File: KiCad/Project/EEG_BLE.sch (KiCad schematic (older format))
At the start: 5 parts

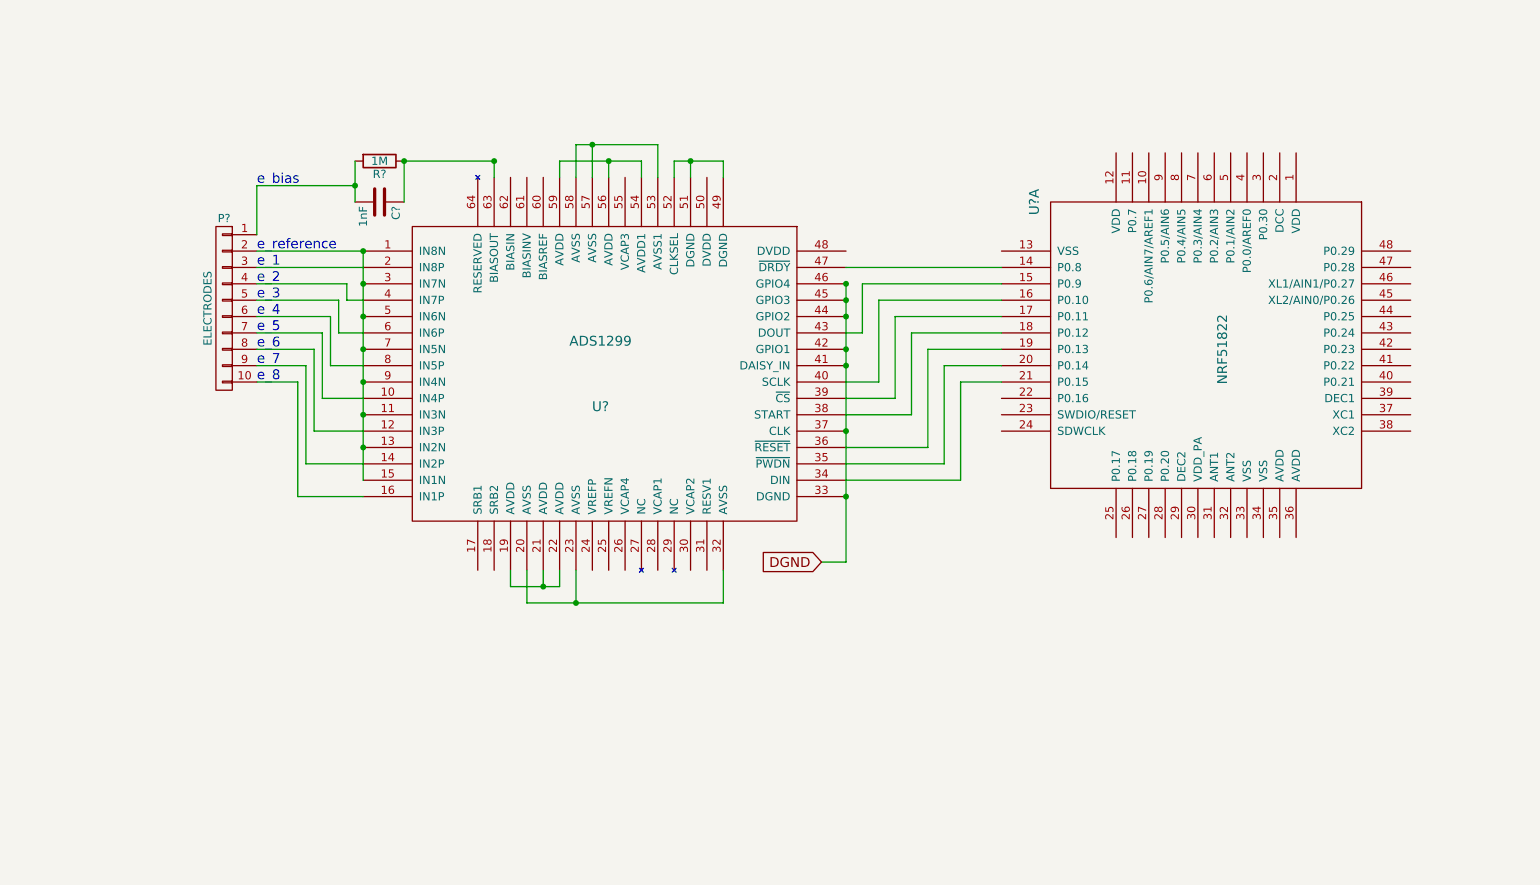
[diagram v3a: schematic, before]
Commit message: Adds decoupling capacitors to the schematics
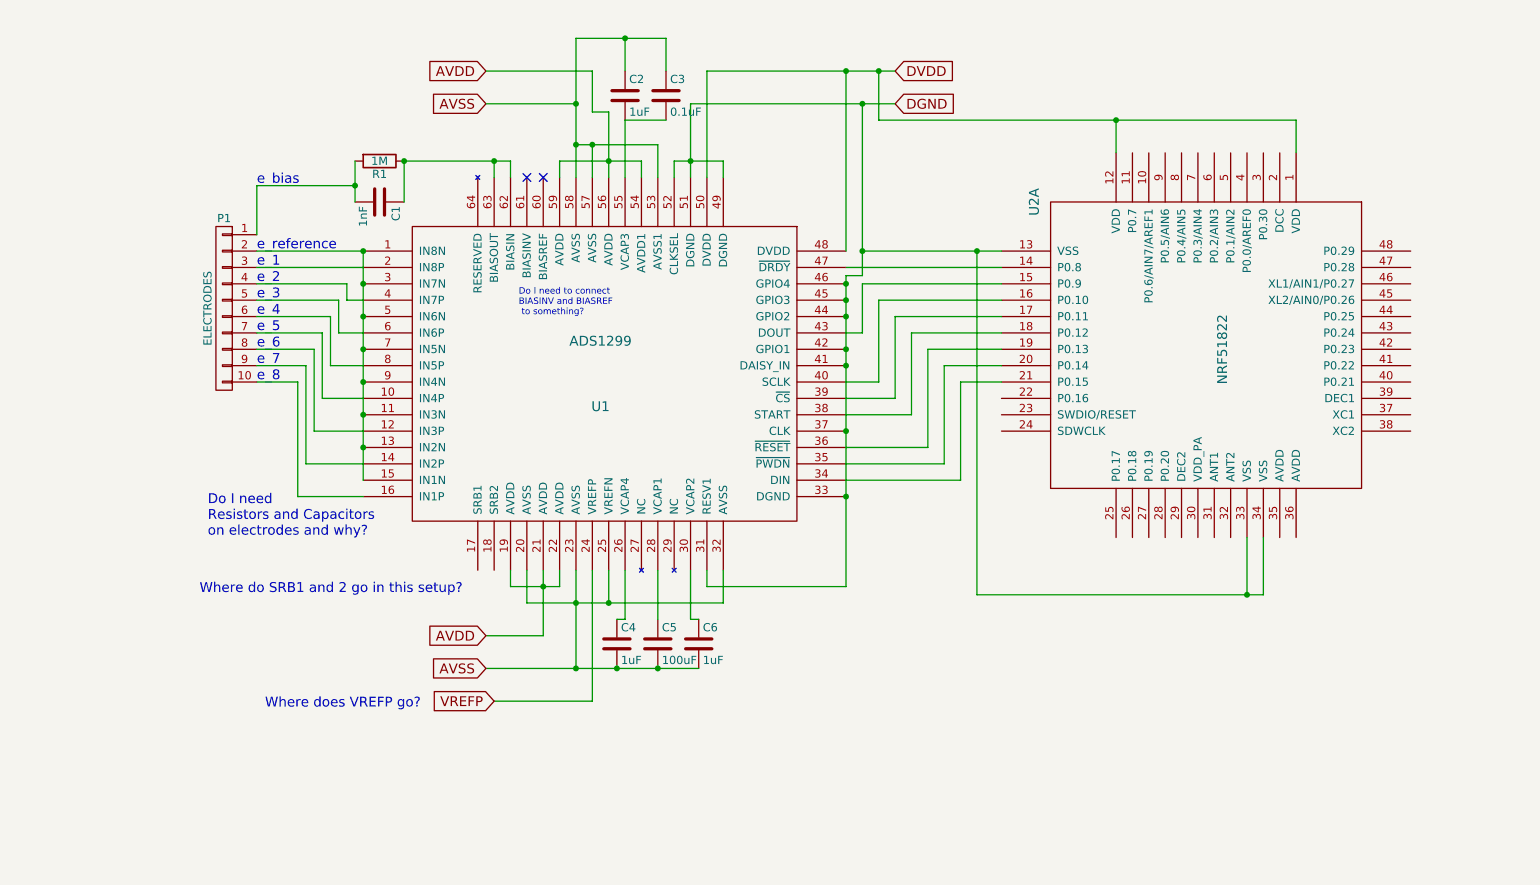
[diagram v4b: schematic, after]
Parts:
- added C2, C4, C6: 1uF, symbol C
- added C3: 0.1uF, symbol C
- added C5: 100uF, symbol C
- gave numbers to parts that had none: 5
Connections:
- net DGND: now also U1.31 (RESV1), U1.49 (DGND), U1.51 (DGND), U1.52 (CLKSEL), U2.13 (VSS), U2.33 (VSS), U2.34 (VSS)
- net AVDD: now reaches U1.19 (AVDD), U1.21 (AVDD), U1.22 (AVDD)
- net AVDD: now also U1.54 (AVDD1), U1.56 (AVDD), U1.59 (AVDD)
- net AVSS: now reaches U1.20 (AVSS), U1.23 (AVSS), U1.32 (AVSS)
- net AVSS: now also U1.25 (VREFN), U1.53 (AVSS1), U1.57 (AVSS), U1.58 (AVSS), C2.1, C3.1, C4.2, C5.2, C6.2
- net VREFP: now reaches U1.24 (VREFP)
- net at U1.26 (VCAP4): now also C4.1
- net at U1.28 (VCAP1): now also C5.1
- net at U1.30 (VCAP2): now also C6.1
- net DVDD: now reaches U1.48 (DVDD)
- net DVDD: now also U1.50 (DVDD), U2.1 (VDD), U2.12 (VDD)
- net at U1.55 (VCAP3): now also C2.2, C3.2
- net at U1.62 (BIASIN): now also C1.1, R1.1, U1.63 (BIASOUT)
- no-connect marks 0 -> 2
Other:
- note added: "Do I need \nResistors and Capacitors \non electrodes and why?"
- note added: "Do I need to connect \nBIASINV and BIASREF\n to something?"
- note added: "Where do SRB1 and 2 go in this setup?"
- note added: "Where does VREFP go?"
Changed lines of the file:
@@
 $EndDescr
 $Comp
-L NRF51822 U?
+L NRF51822 U2
 U 1 1 57D46615
 P 7950 3500
-F 0 "U?" H 6350 2000 60  0000 C CNN
+F 0 "U2" H 6350 2000 60  0000 C CNN
 F 1 "NRF51822" H 7250 3150 60  0000 C CNN
 F 2 "" H 7250 3150 60  0000 C CNN
@@
 $EndComp
 $Comp
-L R R?
+L R R1
 U 1 1 57D49926
 P 2450 1650
-F 0 "R?" V 2530 1650 50  0000 C CNN
+F 0 "R1" V 2530 1650 50  0000 C CNN
 F 1 "1M" V 2450 1650 50  0000 C CNN
 F 2 "" V 2380 1650 50  0000 C CNN
@@
 $EndComp
 $Comp
-L C C?
+L C C1
 U 1 1 57D5BB9F
 P 2450 1900
-F 0 "C?" H 2475 2000 50  0000 L CNN
+F 0 "C1" H 2475 2000 50  0000 L CNN
 F 1 "1nF" H 2475 1800 50  0000 L CNN
 F 2 "" H 2488 1750 50  0000 C CNN
@@
 $EndComp
 $Comp
-L ADS1299 U?
+L ADS1299 U1
 U 1 1 57D3263D
 P 3800 2950
-F 0 "U?" H 3800 2750 60  0000 C CNN
+F 0 "U1" H 3800 2750 60  0000 C CNN
 F 1 "ADS1299" H 3800 3150 60  0000 C CNN
 F 2 "" H 3800 2950 60  0001 C CNN
@@
 $EndComp
 $Comp
-L CONN_01X10 P?
+L CONN_01X10 P1
 U 1 1 57D5C6C1
 P 1500 2550
-F 0 "P?" H 1500 3100 50  0000 C CNN
+F 0 "P1" H 1500 3100 50  0000 C CNN
 F 1 "ELECTRODES" V 1600 2550 50  0000 C CNN
 F 2 "" H 1500 2550 50  0000 C CNN
@@
 Text Notes 1700 1800 0    60   ~ 0
 e_bias
+NoConn ~ 3350 1750
+$Comp
+L C C2
+U 1 1 57DCFDDF
+P 3950 1250
+F 0 "C2" H 3975 1350 50  0000 L CNN
+F 1 "1uF" H 3975 1150 50  0000 L CNN
+F 2 "" H 3988 1100 50  0000 C CNN
+F 3 "" H 3950 1250 50  0000 C CNN
+	1    3950 1250
+	1    0    0    -1
+$EndComp
+$Comp
+L C C4
+U 1 1 57DCFEE7
+P 3900 4600
+F 0 "C4" H 3925 4700 50  0000 L CNN
+F 1 "1uF" H 3925 4500 50  0000 L CNN
+F 2 "" H 3938 4450 50  0000 C CNN
+F 3 "" H 3900 4600 50  0000 C CNN
+	1    3900 4600
+	1    0    0    -1
+$EndComp
+$Comp
+L C C5
+U 1 1 57DCFF14
+P 4150 4600
+F 0 "C5" H 4175 4700 50  0000 L CNN
+F 1 "100uF" H 4175 4500 50  0000 L CNN
+F 2 "" H 4188 4450 50  0000 C CNN
+F 3 "" H 4150 4600 50  0000 C CNN
+	1    4150 4600
+	1    0    0    -1
+$EndComp
+$Comp
+L C C6
+U 1 1 57DCFF41
+P 4400 4600
+F 0 "C6" H 4425 4700 50  0000 L CNN
+F 1 "1uF" H 4425 4500 50  0000 L CNN
+F 2 "" H 4438 4450 50  0000 C CNN
+F 3 "" H 4400 4600 50  0000 C CNN
+	1    4400 4600
+	1    0    0    -1
+$EndComp
+Text GLabel 3100 4550 0    60   Input ~ 0
+AVDD
+Text GLabel 3100 4750 0    60   Input ~ 0
+AVSS
+Text GLabel 5600 1100 2    60   Input ~ 0
+DVDD
+Text GLabel 5600 1300 2    60   Input ~ 0
+DGND
+Text GLabel 3100 1100 0    60   Input ~ 0
+AVDD
+Text GLabel 3100 1300 0    60   Input ~ 0
+AVSS
+NoConn ~ 3450 1750
+$Comp
+L C C3
+U 1 1 57DDBFB3
+P 4200 1250
+F 0 "C3" H 4225 1350 50  0000 L CNN
+F 1 "0.1uF" H 4225 1150 50  0000 L CNN
+F 2 "" H 4238 1100 50  0000 C CNN
+F 3 "" H 4200 1250 50  0000 C CNN
+	1    4200 1250
+	1    0    0    -1
+$EndComp
+Text GLabel 3150 4950 0    60   Input ~ 0
+VREFP
+Connection ~ 7750 4300
+Wire Wire Line
+	7750 3950 7750 4300
+Connection ~ 6100 2200
+Wire Wire Line
+	6100 4300 6100 2200
+Wire Wire Line
+	7850 4300 6100 4300
+Wire Wire Line
+	7850 3950 7850 4300
+Connection ~ 5400 2200
+Wire Wire Line
+	5500 1400 5500 1100
+Connection ~ 6950 1400
+Wire Wire Line
+	6950 1600 6950 1400
+Wire Wire Line
+	8050 1400 5500 1400
+Wire Wire Line
+	8050 1600 8050 1400
+Connection ~ 5500 1100
+Wire Wire Line
+	5400 2200 6250 2200
+Wire Wire Line
+	3750 4950 3150 4950
+Wire Wire Line
+	3750 4150 3750 4950
+Connection ~ 3850 4350
+Wire Wire Line
+	3850 4150 3850 4350
+Wire Wire Line
+	3950 1400 4200 1400
+Connection ~ 3950 900
+Wire Wire Line
+	4200 900  4200 1100
+Wire Wire Line
+	3950 900  3950 1100
+Wire Wire Line
+	3650 900  4200 900
+Connection ~ 3650 1300
+Connection ~ 3900 4750
+Connection ~ 4150 4750
+Connection ~ 3650 4750
+Wire Wire Line
+	3750 1100 3100 1100
+Wire Wire Line
+	3750 1350 3750 1100
+Wire Wire Line
+	3750 1350 3850 1350
+Wire Wire Line
+	3650 1300 3100 1300
+Connection ~ 5400 1300
+Wire Wire Line
+	5400 2350 5400 1300
+Wire Wire Line
+	5300 2350 5400 2350
+Connection ~ 5300 1100
+Wire Wire Line
+	5300 2200 5300 1100
+Wire Wire Line
+	4450 1100 5600 1100
+Wire Wire Line
+	4450 1750 4450 1100
+Wire Wire Line
+	4350 1300 5600 1300
+Wire Wire Line
+	3100 4750 4400 4750
+Wire Wire Line
+	3450 4550 3100 4550
+Wire Wire Line
+	4450 4250 5300 4250
+Wire Wire Line
+	4450 4150 4450 4250
+Wire Wire Line
+	4350 4450 4350 4150
+Wire Wire Line
+	4400 4450 4350 4450
 Connection ~ 2600 1650
 Wire Wire Line
-	3150 1650 2600 1650
+	2600 1650 3250 1650
 Connection ~ 2350 2200
 Connection ~ 2350 2400
@@
 	3250 4250 3550 4250
 Wire Wire Line
-	3450 4250 3450 4150
+	3450 4150 3450 4550
 Wire Wire Line
 	3550 4250 3550 4150
@@
 	3350 4350 4550 4350
 Wire Wire Line
-	3650 4350 3650 4150
+	3650 4150 3650 4750
 Wire Wire Line
 	4550 4350 4550 4150
@@
 	3550 1650 4050 1650
 Wire Wire Line
-	3850 1650 3850 1750
+	3850 1350 3850 1750
 Wire Wire Line
 	4050 1650 4050 1750
 Connection ~ 3850 1650
 Wire Wire Line
-	3650 1750 3650 1550
+	3650 900  3650 1750
 Wire Wire Line
 	3650 1550 4150 1550
@@
 	4550 1650 4550 1750
 Wire Wire Line
-	4350 1750 4350 1650
+	4350 1300 4350 1750
 Connection ~ 4350 1650
 Wire Wire Line
-	5300 2400 5300 4100
-Text GLabel 5150 4100 0    60   Input ~ 0
-DGND
-Wire Wire Line
-	5300 4100 5150 4100
+	5300 2350 5300 4250
+Wire Wire Line
+	3250 1650 3250 1750
+Connection ~ 3650 1550
+Wire Wire Line
+	3950 1750 3950 1400
+Wire Wire Line
+	3900 4450 3950 4450
+Wire Wire Line
+	3950 4450 3950 4150
+Wire Wire Line
+	4150 4450 4150 4150
+Text Notes 1750 5000 0    60   ~ 0
+Where does VREFP go?
+Text Notes 1350 4300 0    60   ~ 0
+Where do SRB1 and 2 go in this setup?
+Text Notes 1400 3950 0    60   ~ 0
+Do I need \nResistors and Capacitors \non electrodes and why?
+Text Notes 3300 2600 0    39   ~ 0
+Do I need to connect \nBIASINV and BIASREF\n to something?
 $EndSCHEMATC

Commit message: Adds questions and power supplies draft
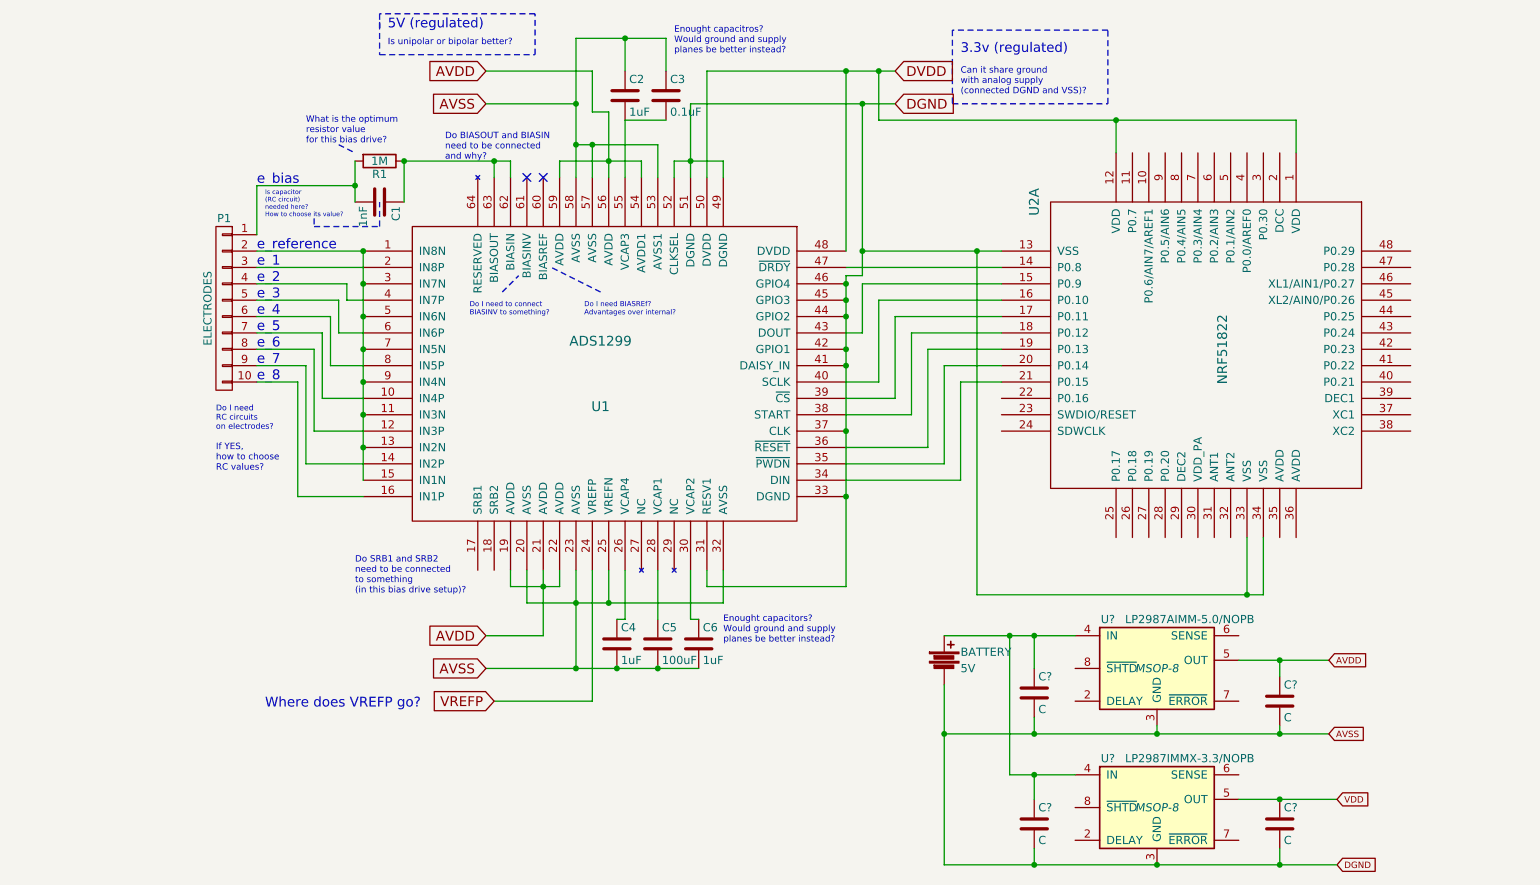
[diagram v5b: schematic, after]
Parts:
- added BATTERY: 5V, symbol Battery
- added C? (x4): C, symbol C
- added U?: LP2987AIMM-5.0/NOPB, MSOP-8, symbol LP2987AIMM-5.0/NOPB
- added U?: LP2987IMMX-3.3/NOPB, MSOP-8, symbol LP2987IMMX-3.3/NOPB
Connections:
- net DGND is gone; now on net AVSS: U1.31 (RESV1), U1.33 (DGND), U1.37 (CLK), U1.41 (DAISY_IN), U1.42 (GPIO1), U1.44 (GPIO2), U1.45 (GPIO3), U1.46 (GPIO4), U1.49 (DGND), U1.51 (DGND), U1.52 (CLKSEL), U2.13 (VSS), U2.33 (VSS), U2.34 (VSS)
- net AVDD: now also C?.1, U?.5 (OUT)
- net AVSS: now also BATTERY.2, C?.2, C?.2, C?.2, C?.2, U?.3 (GND), U?.3 (GND)
- new net: BATTERY.1, C?.1, C?.1, U?.4 (IN), U?.4 (IN)
- new net VDD: C?.1, U?.5 (OUT)
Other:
- note added: "3.3v (regulated)"
- note added: "5V (regulated)"
- note added: "Can it share ground \nwith analog supply \n(connected DGND and VSS)?"
- note added: "Do BIASOUT and BIASIN \nneed to be connected \nand why?"
- note added: "Do I need BIASREf?\nAdvantages over internal?"
- note added: "Do I need \nRC circuits\non electrodes?"
- note added: "Do I need to connect \nBIASINV to something?"
- note added: "Do SRB1 and SRB2 \nneed to be connected \nto something \n(in this bias drive setup)?"
- note added: "Enought capacitors?\nWould ground and supply \nplanes be better instead?"
- note added: "Enought capacitros?\nWould ground and supply \nplanes be better instead?"
- note added: "If YES, \nhow to choose \nRC values?"
- note added: "Is capacitor \n(RC circuit)\nneeded here? \nHow to choose its value?"
- note added: "Is unipolar or bipolar better?"
- note added: "What is the optimum \nresistor value \nfor this bias drive?"
- note removed: "Do I need \nResistors and Capacitors \non electrodes and why?"
- note removed: "Do I need to connect \nBIASINV and BIASREF\n to something?"
- note removed: "Where do SRB1 and 2 go in this setup?"
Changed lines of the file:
@@
-$EndComp
-$Comp
-L ADS1299 U1
-U 1 1 57D3263D
-P 3800 2950
-F 0 "U1" H 3800 2750 60  0000 C CNN
-F 1 "ADS1299" H 3800 3150 60  0000 C CNN
-F 2 "" H 3800 2950 60  0001 C CNN
-F 3 "" H 3800 2950 60  0001 C CNN
-	1    3800 2950
-	1    0    0    -1
 $EndComp
 $Comp
@@
 Connection ~ 4350 1650
 Wire Wire Line
-	5300 2350 5300 4250
+	5300 4250 5300 2350
 Wire Wire Line
 	3250 1650 3250 1750
@@
 Text Notes 1750 5000 0    60   ~ 0
 Where does VREFP go?
-Text Notes 1350 4300 0    60   ~ 0
-Where do SRB1 and 2 go in this setup?
-Text Notes 1400 3950 0    60   ~ 0
-Do I need \nResistors and Capacitors \non electrodes and why?
-Text Notes 3300 2600 0    39   ~ 0
-Do I need to connect \nBIASINV and BIASREF\n to something?
+Text Notes 2300 4300 0    39   ~ 0
+Do SRB1 and SRB2 \nneed to be connected \nto something \n(in this bias drive setup)?
+Text Notes 1450 3300 0    35   ~ 0
+Do I need \nRC circuits\non electrodes?
+Text Notes 3000 2600 0    31   ~ 0
+Do I need to connect \nBIASINV to something?
+Text Notes 2850 1650 0    39   ~ 0
+Do BIASOUT and BIASIN \nneed to be connected \nand why?
+Text Notes 2000 1550 0    39   ~ 0
+What is the optimum \nresistor value \nfor this bias drive?
+Wire Notes Line
+	2200 1550 2300 1600
+Text Notes 6000 1000 0    59   ~ 0
+3.3v (regulated)
+Text Notes 2500 850  0    59   ~ 0
+5V (regulated)
+$Comp
+L Battery BATTERY
+U 1 1 57DE7944
+P 5900 4700
+F 0 "BATTERY" H 6000 4750 50  0000 L CNN
+F 1 "5V" H 6000 4650 50  0000 L CNN
+F 2 "" V 5900 4740 50  0000 C CNN
+F 3 "" V 5900 4740 50  0000 C CNN
+	1    5900 4700
+	1    0    0    -1
+$EndComp
+$Comp
+L ADS1299 U1
+U 1 1 57D3263D
+P 3800 2950
+F 0 "U1" H 3800 2750 60  0000 C CNN
+F 1 "ADS1299" H 3800 3150 60  0000 C CNN
+F 2 "" H 3800 2950 60  0001 C CNN
+F 3 "" H 3800 2950 60  0001 C CNN
+	1    3800 2950
+	1    0    0    -1
+$EndComp
+Text Notes 3700 2600 0    31   ~ 0
+Do I need BIASREf?\nAdvantages over internal?
+Wire Notes Line
+	3800 2450 3500 2300
+Wire Notes Line
+	3200 2450 3300 2350
+Text Notes 2500 950  0    39   ~ 0
+Is unipolar or bipolar better?
+Wire Notes Line
+	2450 750  2450 1000
+Wire Notes Line
+	2450 1000 3400 1000
+Wire Notes Line
+	3400 1000 3400 750
+Wire Notes Line
+	3400 750  2450 750
+Wire Notes Line
+	2450 800  2450 850
+Text Notes 6000 1250 0    39   ~ 0
+Can it share ground \nwith analog supply \n(connected DGND and VSS)?
+Wire Notes Line
+	5950 850  5950 1300
+Wire Notes Line
+	5950 1300 6900 1300
+Wire Notes Line
+	6900 1300 6900 850
+Wire Notes Line
+	6900 850  5950 850
+Text Notes 1750 2000 0    28   ~ 0
+Is capacitor \n(RC circuit)\nneeded here? \nHow to choose its value?
+Wire Notes Line
+	2050 2000 2050 2050
+Wire Notes Line
+	2050 2050 2450 2050
+Wire Notes Line
+	2450 2050 2450 1900
+Text Notes 1450 3550 0    39   ~ 0
+If YES, \nhow to choose \nRC values?
+Text Notes 4550 4600 0    39   ~ 0
+Enought capacitors?\nWould ground and supply \nplanes be better instead?
+Text Notes 4250 1000 0    39   ~ 0
+Enought capacitros?\nWould ground and supply \nplanes be better instead?
+Wire Wire Line
+	5900 4550 6700 4550
+$Comp
+L LP2987AIMM-5.0/NOPB U?
+U 1 1 57DE8D4A
+P 7200 4750
+F 0 "U?" H 6900 5050 50  0000 C CNN
+F 1 "LP2987AIMM-5.0/NOPB" H 7400 5050 50  0000 C CNN
+F 2 "MSOP-8" H 7200 4750 50  0000 C CIN
+F 3 "" H 7200 4750 50  0000 C CNN
+	1    7200 4750
+	1    0    0    -1
+$EndComp
+Wire Wire Line
+	5900 4850 5900 5950
+Wire Wire Line
+	5900 5150 8250 5150
+Wire Wire Line
+	7200 5150 7200 5100
+Connection ~ 7200 5150
+Wire Wire Line
+	7700 4700 8250 4700
+$Comp
+L C C?
+U 1 1 57DE8FE2
+P 7950 4950
+F 0 "C?" H 7975 5050 50  0000 L CNN
+F 1 "C" H 7975 4850 50  0000 L CNN
+F 2 "" H 7988 4800 50  0000 C CNN
+F 3 "" H 7950 4950 50  0000 C CNN
+	1    7950 4950
+	1    0    0    -1
+$EndComp
+Wire Wire Line
+	7950 4800 7950 4700
+Connection ~ 7950 4700
+Wire Wire Line
+	7950 5100 7950 5150
+Connection ~ 7950 5150
+$Comp
+L C C?
+U 1 1 57DE91C6
+P 6450 4900
+F 0 "C?" H 6475 5000 50  0000 L CNN
+F 1 "C" H 6475 4800 50  0000 L CNN
+F 2 "" H 6488 4750 50  0000 C CNN
+F 3 "" H 6450 4900 50  0000 C CNN
+	1    6450 4900
+	1    0    0    -1
+$EndComp
+Wire Wire Line
+	6450 4550 6450 4750
+Connection ~ 6450 4550
+Wire Wire Line
+	6450 5050 6450 5150
+Connection ~ 6450 5150
+Text GLabel 8250 4700 2    39   Input ~ 0
+AVDD
+Text GLabel 8250 5150 2    39   Input ~ 0
+AVSS
+$Comp
+L LP2987IMMX-3.3/NOPB U?
+U 1 1 57DE9BCA
+P 7200 5600
+F 0 "U?" H 6900 5900 50  0000 C CNN
+F 1 "LP2987IMMX-3.3/NOPB" H 7400 5900 50  0000 C CNN
+F 2 "MSOP-8" H 7200 5600 50  0000 C CIN
+F 3 "" H 7200 5600 50  0000 C CNN
+	1    7200 5600
+	1    0    0    -1
+$EndComp
+Connection ~ 5900 5150
+Wire Wire Line
+	6300 4550 6300 5400
+Wire Wire Line
+	6300 5400 6700 5400
+Connection ~ 6300 4550
+$Comp
+L C C?
+U 1 1 57DE9DA6
+P 6450 5700
+F 0 "C?" H 6475 5800 50  0000 L CNN
+F 1 "C" H 6475 5600 50  0000 L CNN
+F 2 "" H 6488 5550 50  0000 C CNN
+F 3 "" H 6450 5700 50  0000 C CNN
+	1    6450 5700
+	1    0    0    -1
+$EndComp
+$Comp
+L C C?
+U 1 1 57DE9DFA
+P 7950 5700
+F 0 "C?" H 7975 5800 50  0000 L CNN
+F 1 "C" H 7975 5600 50  0000 L CNN
+F 2 "" H 7988 5550 50  0000 C CNN
+F 3 "" H 7950 5700 50  0000 C CNN
+	1    7950 5700
+	1    0    0    -1
+$EndComp
+Wire Wire Line
+	6450 5550 6450 5400
+Connection ~ 6450 5400
+Wire Wire Line
+	6450 5850 6450 5950
+Connection ~ 6450 5950
+Connection ~ 7200 5950
+Wire Wire Line
+	7700 5550 8300 5550
+Wire Wire Line
+	5900 5950 8300 5950
+Wire Wire Line
+	7950 5850 7950 5950
+Connection ~ 7950 5950
+Connection ~ 7950 5550
+Text GLabel 8300 5550 2    39   Input ~ 0
+VDD
+Text GLabel 8300 5950 2    39   Input ~ 0
+DGND
 $EndSCHEMATC
